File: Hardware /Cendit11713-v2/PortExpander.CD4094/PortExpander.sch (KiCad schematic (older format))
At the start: 4 parts

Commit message: Cendit 11713 port expander CD4094 + respaldo
 - Inicia esquematico y PCB para IO expander con SR CD4094
 - Respaldo de software
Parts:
- added C3, C4, C5: C, Capacitors_SMD:C_0805_HandSoldering, symbol C
- added P1: CONN_01X06, Pin_Headers:Pin_Header_Straight_1x06, symbol CONN_01X06
- added P2, P3: CONN_01X07, Pin_Headers:Pin_Header_Straight_1x07, symbol CONN_01X07
- added R1, R2: 10k, Resistors_SMD:R_0805_HandSoldering, symbol R_Small
- added U3: CD4094BE, CenditFootprints2:CD4094-DIP16, symbol CD4094BE
- added U4: ULN2003A, CenditFootprints2:ULN2003-DIP16, symbol ULN2003A-RESCUE-PortExpander
- C1, C2: renamed from C?; footprint (none) -> Capacitors_SMD:C_0805_HandSoldering
- U1: renamed from U?; footprint DIP254P762X508-16 -> CenditFootprints2:CD4094-DIP16
- U2: renamed from U?; footprint (none) -> CenditFootprints2:ULN2003-DIP16; symbol ULN2003A -> ULN2003A-RESCUE-PortExpander
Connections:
- net GNDPWR: now also C1.2, C2.2, U1.8 (VSS), U2.8 (GND), C3.2, C4.2, C5.2, U3.8 (VSS), U4.8 (GND)
- net VDD: now also C1.1, C2.1, U1.16 (VDD), U2.9 (COM), C3.1, C4.1, C5.1, R1.2, R2.2, U3.16 (VDD), U4.9 (COM)
- net STRB: now reaches U1.1 (STRB)
- net STRB: now also U3.1 (STRB)
- net at U1.12 (Q7): now also U2.7 (I7)
- net at U1.13 (Q6): now also U2.6 (I6)
- net at U1.14 (Q5): now also U2.5 (I5)
- net OE: now reaches U1.15 (OUT_EN)
- net OE: now also R1.1, R2.1, U3.15 (OUT_EN)
- net DATA: now reaches U1.2 (DATA)
- net CLK: now reaches U1.3 (CLOCK)
- net CLK: now also U3.3 (CLOCK)
- net at U1.4 (Q1): now also U2.1 (I1)
- net at U1.5 (Q2): now also U2.2 (I2)
- net at U1.6 (Q3): now also U2.3 (I3)
- net at U1.7 (Q4): now also U2.4 (I4)
- net at U1.9 (QS): now also U3.2 (DATA)
- net P6: now reaches U2.10 (O7)
- net P6: now also P2.7 (P7)
- net P5: now reaches U2.11 (O6)
- net P5: now also P2.6 (P6)
- net P4: now reaches U2.12 (O5)
- net P4: now also P2.5 (P5)
- net P3: now reaches U2.13 (O4)
- net P3: now also P2.4 (P4)
- net P2: now reaches U2.14 (O3)
- net P2: now also P2.3 (P3)
- net P1: now reaches U2.15 (O2)
- net P1: now also P2.2 (P2)
- net P0: now reaches U2.16 (O1)
- net P0: now also P2.1 (P1)
- new net: U3.12 (Q7), U4.7 (I7)
- new net: U3.13 (Q6), U4.6 (I6)
- new net: U3.14 (Q5), U4.5 (I5)
- new net: U3.4 (Q1), U4.1 (I1)
- new net: U3.5 (Q2), U4.2 (I2)
- new net: U3.6 (Q3), U4.3 (I3)
- new net: U3.7 (Q4), U4.4 (I4)
- new net P10: P3.4 (P4), U4.13 (O4)
- new net P11: P3.5 (P5), U4.12 (O5)
- new net P12: P3.6 (P6), U4.11 (O6)
- new net P13: P3.7 (P7), U4.10 (O7)
- new net P7: P3.1 (P1), U4.16 (O1)
- new net P8: P3.2 (P2), U4.15 (O2)
- new net P9: P3.3 (P3), U4.14 (O3)
- no-connect marks 0 -> 5
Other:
- moved on the sheet: U1, U2

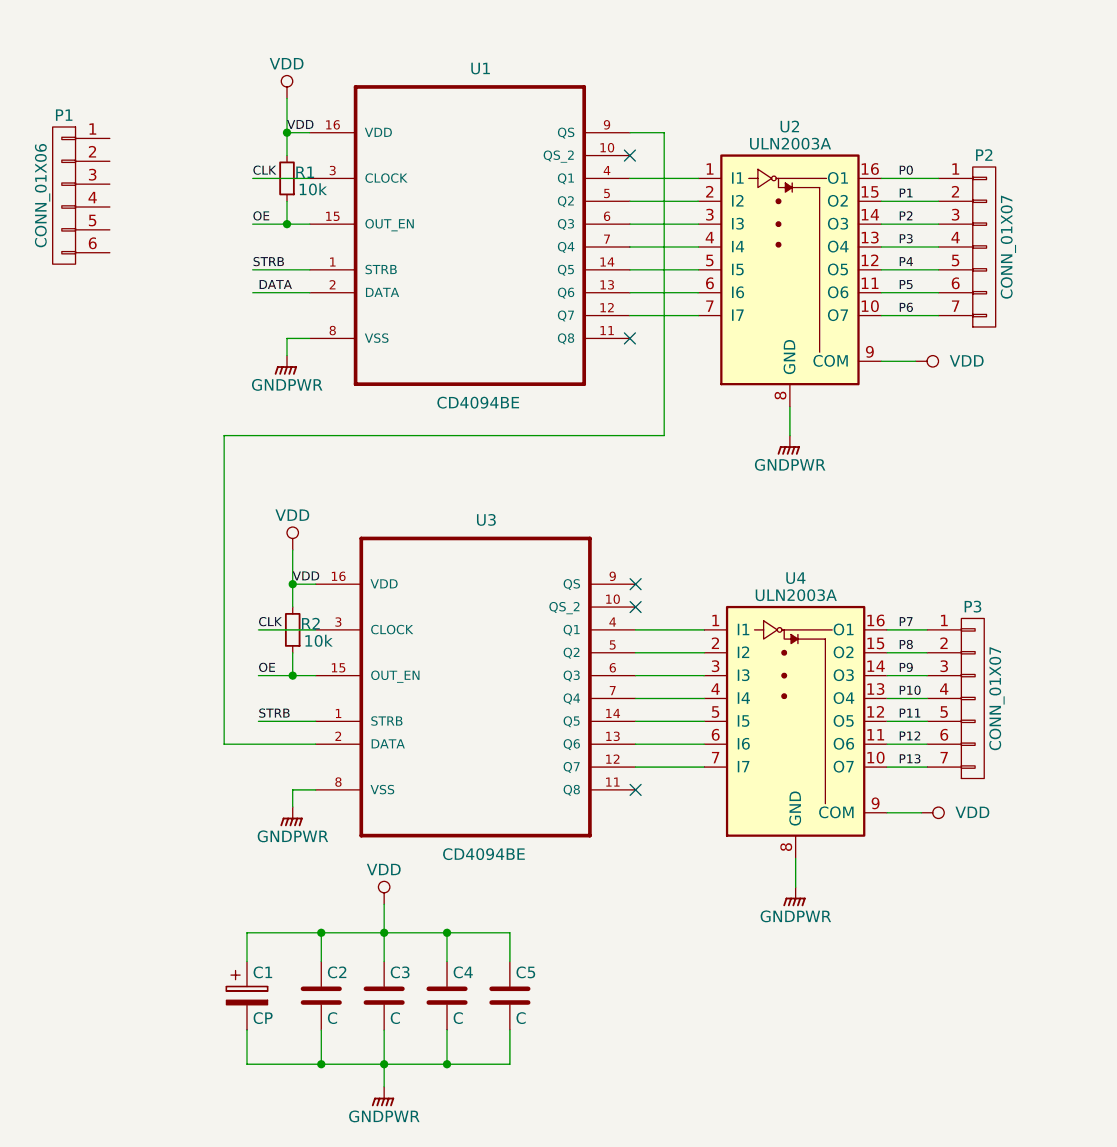
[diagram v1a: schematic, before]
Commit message: En Cendit11713 + CenditLab respaldo
  - Se revisan tarjetas
  - Correccion en PCB GPIB
  - Se inicia tarjeta madre en una pieza (MainBoard.OnePiece)
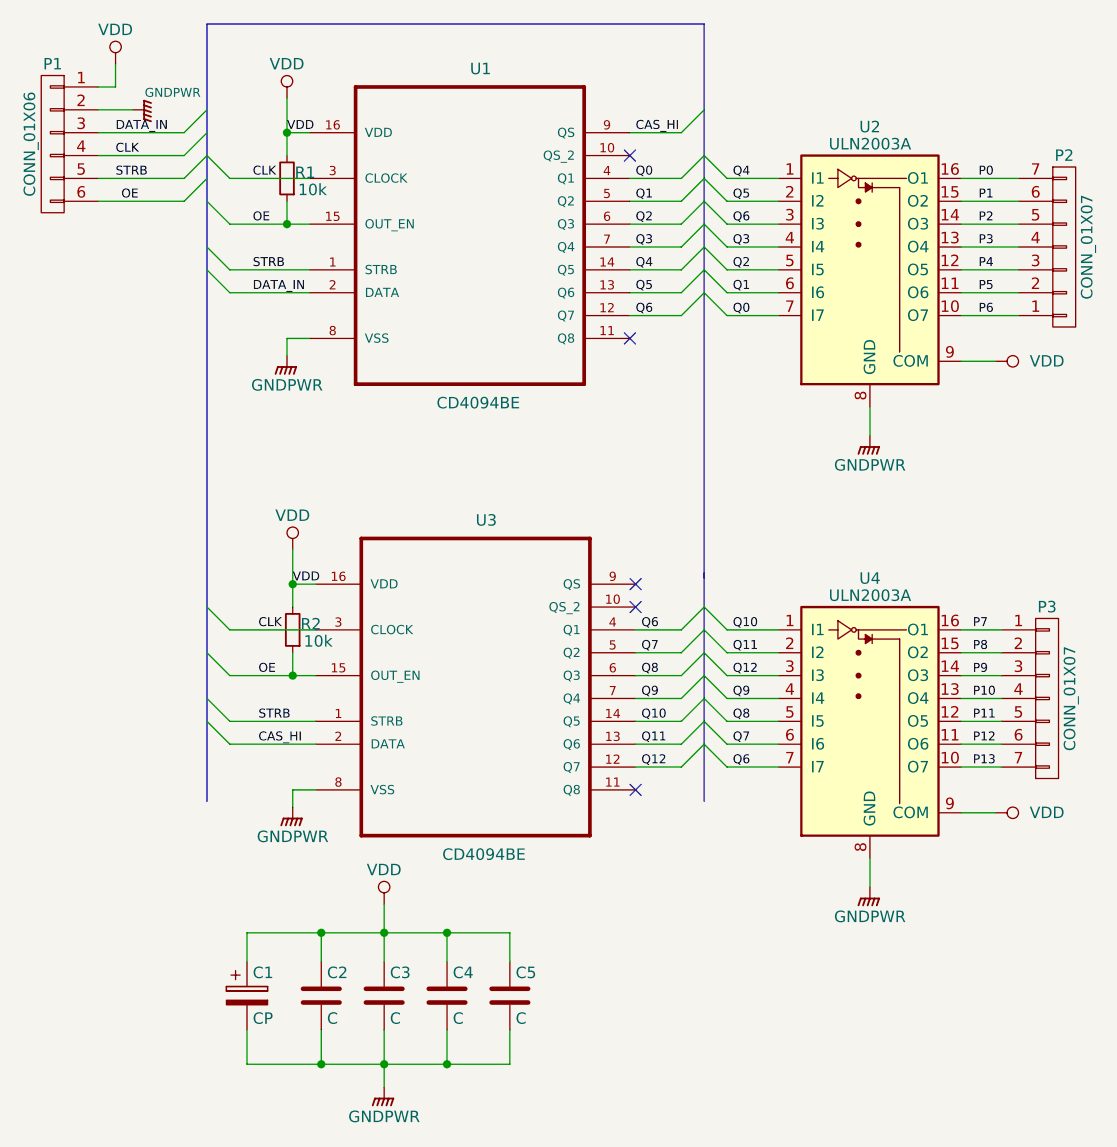
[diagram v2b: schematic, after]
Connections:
- net DATA is gone; now on net DATA_IN: U1.2 (DATA)
- net CLK: now also P1.4 (P4)
- net GNDPWR: now also P1.2 (P2)
- net OE: now also P1.6 (P6)
- net P0: now also P2.7 (P7); no longer P2.1 (P1)
- net P1: now also P2.6 (P6); no longer P2.2 (P2)
- net P2: now also P2.5 (P5); no longer P2.3 (P3)
- net P4: now also P2.3 (P3); no longer P2.5 (P5)
- net P5: now also P2.2 (P2); no longer P2.6 (P6)
- net P6: now also P2.1 (P1); no longer P2.7 (P7)
- net STRB: now also P1.5 (P5)
- net VDD: now also P1.1 (P1)
- net Q0: now reaches U2.7 (I7)
- net Q0: now also U1.4 (Q1); no longer U1.12 (Q7)
- net Q1: now reaches U2.6 (I6)
- net Q1: now also U1.5 (Q2); no longer U1.13 (Q6)
- net Q2: now reaches U2.5 (I5)
- net Q2: now also U1.6 (Q3); no longer U1.14 (Q5)
- net Q4: now reaches U2.1 (I1)
- net Q4: now also U1.14 (Q5); no longer U1.4 (Q1)
- net Q5: now reaches U2.2 (I2)
- net Q5: now also U1.13 (Q6); no longer U1.5 (Q2)
- net Q6: now reaches U2.3 (I3)
- net Q6: now also U1.12 (Q7), U3.4 (Q1), U4.7 (I7); no longer U1.6 (Q3)
- net Q3: now reaches U1.7 (Q4), U2.4 (I4)
- net CAS_HI: now reaches U1.9 (QS), U3.2 (DATA)
- net DATA_IN: now reaches P1.3 (P3)
- net Q12: now reaches U3.12 (Q7)
- net Q12: now also U4.3 (I3); no longer U4.7 (I7)
- net Q11: now reaches U3.13 (Q6)
- net Q11: now also U4.2 (I2); no longer U4.6 (I6)
- net Q10: now reaches U3.14 (Q5)
- net Q10: now also U4.1 (I1); no longer U4.5 (I5)
- net Q7: now reaches U3.5 (Q2)
- net Q7: now also U4.6 (I6); no longer U4.2 (I2)
- net Q8: now reaches U3.6 (Q3)
- net Q8: now also U4.5 (I5); no longer U4.3 (I3)
- net Q9: now reaches U3.7 (Q4), U4.4 (I4)
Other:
- moved on the sheet: P1, P2, P3, U2, U4
